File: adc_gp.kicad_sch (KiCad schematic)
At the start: 69 parts

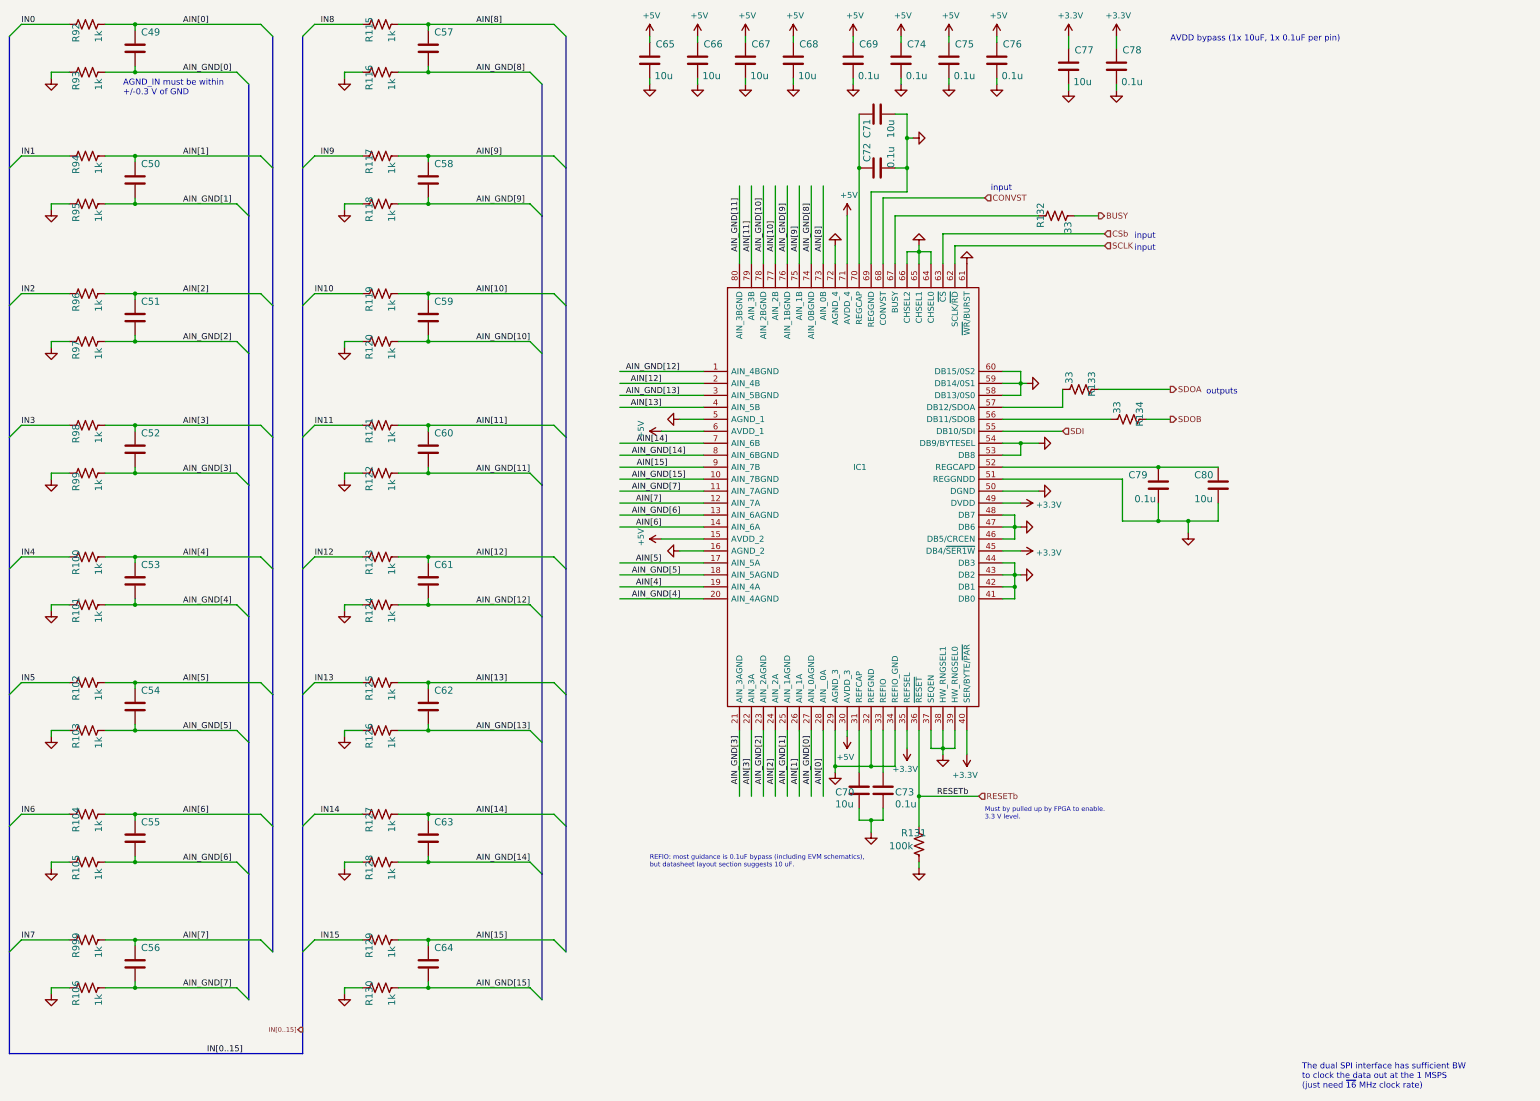
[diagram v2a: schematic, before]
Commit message: Closes #29 full-scale range will be nearly 8uA
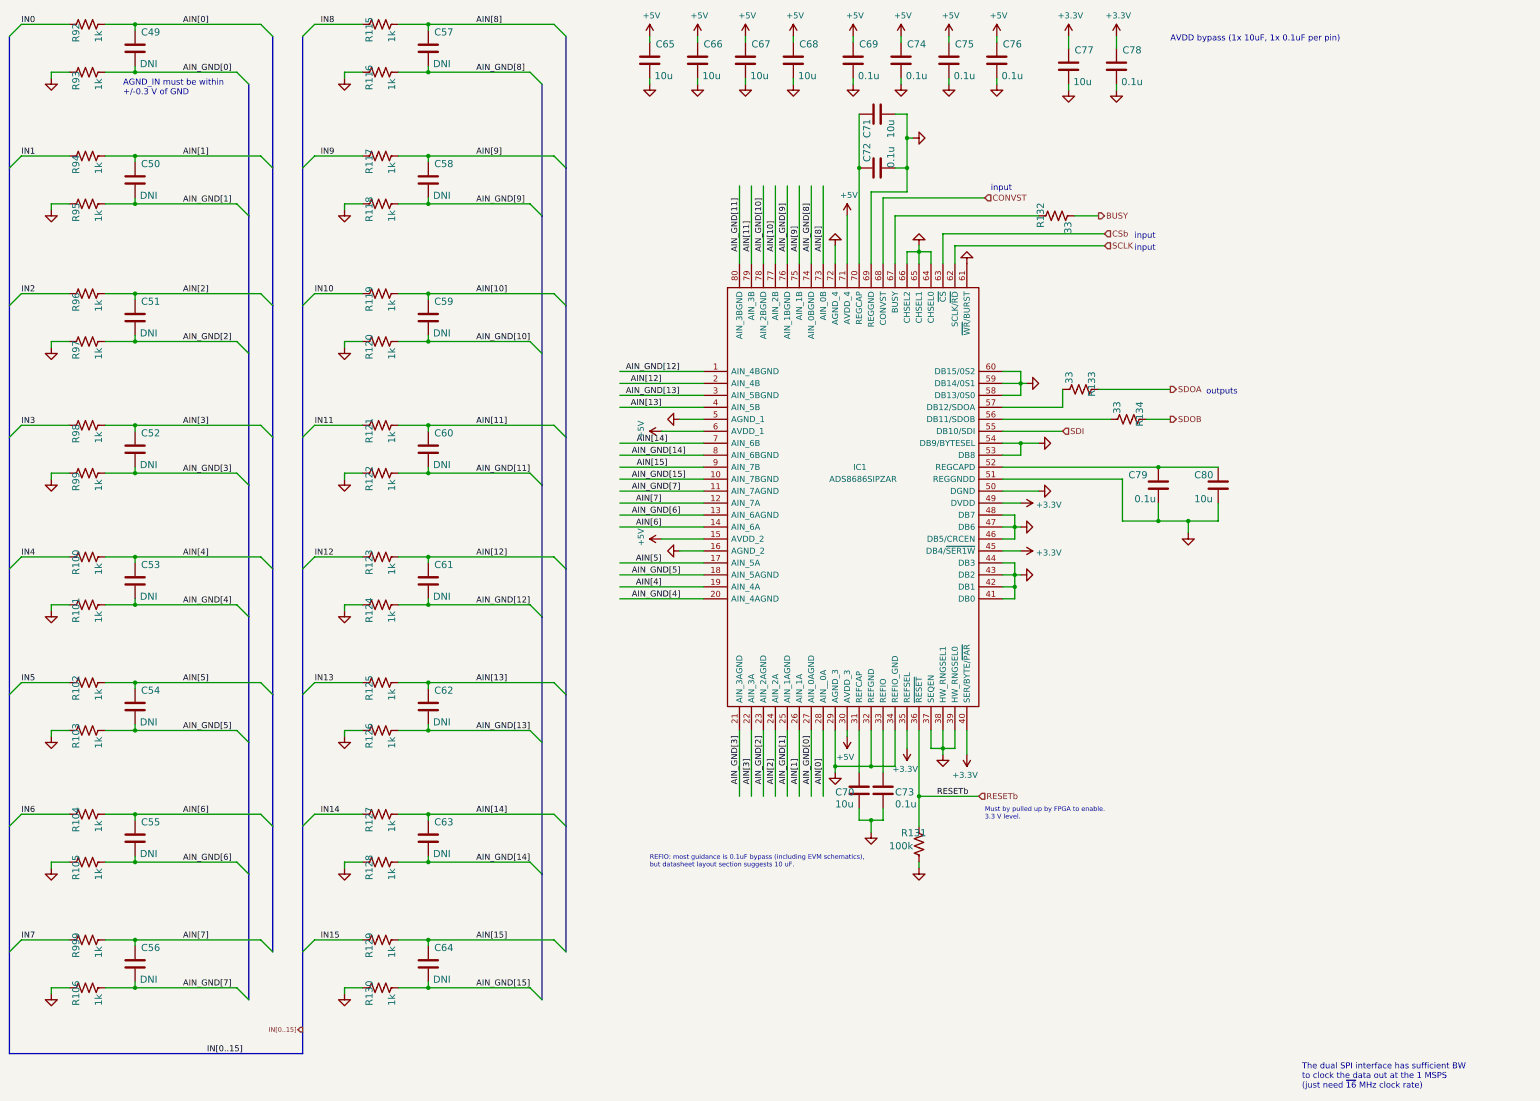
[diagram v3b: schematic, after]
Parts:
- C49, C50, C51, C52, C53, C54, C55, C56, C57, C58, C59, C60, C61, C62, C63, C64: value (none) -> DNI; footprint (none) -> Capacitor_SMD:C_0603_1608Metric
- IC1: value (none) -> ADS8686SIPZAR; footprint (none) -> Package_QFP:LQFP-80_14x14mm_P0.65mm
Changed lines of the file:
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@@
       (effects (font (size 1.27 1.27)) (justify left))
     )
-    (property "Value" "" (id 1) (at 189.23 111.76 0)
+    (property "Value" "ADS8686SIPZAR" (id 1) (at 189.23 111.76 0)
       (effects (font (size 1.27 1.27)) (justify left))
     )
-    (property "Footprint" "" (id 2) (at 222.25 71.12 0)
+    (property "Footprint" "Package_QFP:LQFP-80_14x14mm_P0.65mm" (id 2) (at 222.25 71.12 0)
       (effects (font (size 1.27 1.27)) (justify left) hide)
     )
@@
       (effects (font (size 1.4986 1.4986)) (justify left bottom))
     )
-    (property "Value" "" (id 1) (at 42.926 218.821 0)
-      (effects (font (size 1.4986 1.4986)) (justify left bottom))
-    )
-    (property "Footprint" "" (id 2) (at 41.91 214.63 0)
+    (property "Value" "DNI" (id 1) (at 42.926 218.821 0)
+      (effects (font (size 1.4986 1.4986)) (justify left bottom))
+    )
+    (property "Footprint" "Capacitor_SMD:C_0603_1608Metric" (id 2) (at 41.91 214.63 0)
       (effects (font (size 1.27 1.27)) hide)
     )
@@
       (effects (font (size 1.4986 1.4986)) (justify left bottom))
     )
-    (property "Value" "" (id 1) (at 42.926 192.151 0)
-      (effects (font (size 1.4986 1.4986)) (justify left bottom))
-    )
-    (property "Footprint" "" (id 2) (at 41.91 187.96 0)
+    (property "Value" "DNI" (id 1) (at 42.926 192.151 0)
+      (effects (font (size 1.4986 1.4986)) (justify left bottom))
+    )
+    (property "Footprint" "Capacitor_SMD:C_0603_1608Metric" (id 2) (at 41.91 187.96 0)
       (effects (font (size 1.27 1.27)) hide)
     )
@@
       (effects (font (size 1.4986 1.4986)) (justify left bottom))
     )
-    (property "Value" "" (id 1) (at 42.926 164.211 0)
-      (effects (font (size 1.4986 1.4986)) (justify left bottom))
-    )
-    (property "Footprint" "" (id 2) (at 41.91 160.02 0)
+    (property "Value" "DNI" (id 1) (at 42.926 164.211 0)
+      (effects (font (size 1.4986 1.4986)) (justify left bottom))
+    )
+    (property "Footprint" "Capacitor_SMD:C_0603_1608Metric" (id 2) (at 41.91 160.02 0)
       (effects (font (size 1.27 1.27)) hide)
     )
@@
       (effects (font (size 1.4986 1.4986)) (justify left bottom))
     )
-    (property "Value" "" (id 1) (at 42.926 137.541 0)
-      (effects (font (size 1.4986 1.4986)) (justify left bottom))
-    )
-    (property "Footprint" "" (id 2) (at 41.91 133.35 0)
+    (property "Value" "DNI" (id 1) (at 42.926 137.541 0)
+      (effects (font (size 1.4986 1.4986)) (justify left bottom))
+    )
+    (property "Footprint" "Capacitor_SMD:C_0603_1608Metric" (id 2) (at 41.91 133.35 0)
       (effects (font (size 1.27 1.27)) hide)
     )
@@
       (effects (font (size 1.4986 1.4986)) (justify left bottom))
     )
-    (property "Value" "" (id 1) (at 42.926 109.601 0)
-      (effects (font (size 1.4986 1.4986)) (justify left bottom))
-    )
-    (property "Footprint" "" (id 2) (at 41.91 105.41 0)
+    (property "Value" "DNI" (id 1) (at 42.926 109.601 0)
+      (effects (font (size 1.4986 1.4986)) (justify left bottom))
+    )
+    (property "Footprint" "Capacitor_SMD:C_0603_1608Metric" (id 2) (at 41.91 105.41 0)
       (effects (font (size 1.27 1.27)) hide)
     )
@@
       (effects (font (size 1.4986 1.4986)) (justify left bottom))
     )
-    (property "Value" "" (id 1) (at 42.926 81.661 0)
-      (effects (font (size 1.4986 1.4986)) (justify left bottom))
-    )
-    (property "Footprint" "" (id 2) (at 41.91 77.47 0)
+    (property "Value" "DNI" (id 1) (at 42.926 81.661 0)
+      (effects (font (size 1.4986 1.4986)) (justify left bottom))
+    )
+    (property "Footprint" "Capacitor_SMD:C_0603_1608Metric" (id 2) (at 41.91 77.47 0)
       (effects (font (size 1.27 1.27)) hide)
     )
@@
       (effects (font (size 1.4986 1.4986)) (justify left bottom))
     )
-    (property "Value" "" (id 1) (at 42.926 52.451 0)
-      (effects (font (size 1.4986 1.4986)) (justify left bottom))
-    )
-    (property "Footprint" "" (id 2) (at 41.91 48.26 0)
+    (property "Value" "DNI" (id 1) (at 42.926 52.451 0)
+      (effects (font (size 1.4986 1.4986)) (justify left bottom))
+    )
+    (property "Footprint" "Capacitor_SMD:C_0603_1608Metric" (id 2) (at 41.91 48.26 0)
       (effects (font (size 1.27 1.27)) hide)
     )
@@
       (effects (font (size 1.4986 1.4986)) (justify left bottom))
     )
-    (property "Value" "" (id 1) (at 42.926 24.511 0)
-      (effects (font (size 1.4986 1.4986)) (justify left bottom))
-    )
-    (property "Footprint" "" (id 2) (at 41.91 20.32 0)
+    (property "Value" "DNI" (id 1) (at 42.926 24.511 0)
+      (effects (font (size 1.4986 1.4986)) (justify left bottom))
+    )
+    (property "Footprint" "Capacitor_SMD:C_0603_1608Metric" (id 2) (at 41.91 20.32 0)
       (effects (font (size 1.27 1.27)) hide)
     )
@@
       (effects (font (size 1.4986 1.4986)) (justify left bottom))
     )
-    (property "Value" "" (id 1) (at 105.156 218.821 0)
-      (effects (font (size 1.4986 1.4986)) (justify left bottom))
-    )
-    (property "Footprint" "" (id 2) (at 104.14 214.63 0)
+    (property "Value" "DNI" (id 1) (at 105.156 218.821 0)
+      (effects (font (size 1.4986 1.4986)) (justify left bottom))
+    )
+    (property "Footprint" "Capacitor_SMD:C_0603_1608Metric" (id 2) (at 104.14 214.63 0)
       (effects (font (size 1.27 1.27)) hide)
     )
@@
       (effects (font (size 1.4986 1.4986)) (justify left bottom))
     )
-    (property "Value" "" (id 1) (at 105.156 192.151 0)
-      (effects (font (size 1.4986 1.4986)) (justify left bottom))
-    )
-    (property "Footprint" "" (id 2) (at 104.14 187.96 0)
+    (property "Value" "DNI" (id 1) (at 105.156 192.151 0)
+      (effects (font (size 1.4986 1.4986)) (justify left bottom))
+    )
+    (property "Footprint" "Capacitor_SMD:C_0603_1608Metric" (id 2) (at 104.14 187.96 0)
       (effects (font (size 1.27 1.27)) hide)
     )
@@
       (effects (font (size 1.4986 1.4986)) (justify left bottom))
     )
-    (property "Value" "" (id 1) (at 105.156 164.211 0)
-      (effects (font (size 1.4986 1.4986)) (justify left bottom))
-    )
-    (property "Footprint" "" (id 2) (at 104.14 160.02 0)
+    (property "Value" "DNI" (id 1) (at 105.156 164.211 0)
+      (effects (font (size 1.4986 1.4986)) (justify left bottom))
+    )
+    (property "Footprint" "Capacitor_SMD:C_0603_1608Metric" (id 2) (at 104.14 160.02 0)
       (effects (font (size 1.27 1.27)) hide)
     )
@@
       (effects (font (size 1.4986 1.4986)) (justify left bottom))
     )
-    (property "Value" "" (id 1) (at 105.156 137.541 0)
-      (effects (font (size 1.4986 1.4986)) (justify left bottom))
-    )
-    (property "Footprint" "" (id 2) (at 104.14 133.35 0)
+    (property "Value" "DNI" (id 1) (at 105.156 137.541 0)
+      (effects (font (size 1.4986 1.4986)) (justify left bottom))
+    )
+    (property "Footprint" "Capacitor_SMD:C_0603_1608Metric" (id 2) (at 104.14 133.35 0)
       (effects (font (size 1.27 1.27)) hide)
     )
@@
       (effects (font (size 1.4986 1.4986)) (justify left bottom))
     )
-    (property "Value" "" (id 1) (at 105.156 109.601 0)
-      (effects (font (size 1.4986 1.4986)) (justify left bottom))
-    )
-    (property "Footprint" "" (id 2) (at 104.14 105.41 0)
+    (property "Value" "DNI" (id 1) (at 105.156 109.601 0)
+      (effects (font (size 1.4986 1.4986)) (justify left bottom))
+    )
+    (property "Footprint" "Capacitor_SMD:C_0603_1608Metric" (id 2) (at 104.14 105.41 0)
       (effects (font (size 1.27 1.27)) hide)
     )
@@
       (effects (font (size 1.4986 1.4986)) (justify left bottom))
     )
-    (property "Value" "" (id 1) (at 105.156 81.661 0)
-      (effects (font (size 1.4986 1.4986)) (justify left bottom))
-    )
-    (property "Footprint" "" (id 2) (at 104.14 77.47 0)
+    (property "Value" "DNI" (id 1) (at 105.156 81.661 0)
+      (effects (font (size 1.4986 1.4986)) (justify left bottom))
+    )
+    (property "Footprint" "Capacitor_SMD:C_0603_1608Metric" (id 2) (at 104.14 77.47 0)
       (effects (font (size 1.27 1.27)) hide)
     )
@@
       (effects (font (size 1.4986 1.4986)) (justify left bottom))
     )
-    (property "Value" "" (id 1) (at 105.156 52.451 0)
-      (effects (font (size 1.4986 1.4986)) (justify left bottom))
-    )
-    (property "Footprint" "" (id 2) (at 104.14 48.26 0)
+    (property "Value" "DNI" (id 1) (at 105.156 52.451 0)
+      (effects (font (size 1.4986 1.4986)) (justify left bottom))
+    )
+    (property "Footprint" "Capacitor_SMD:C_0603_1608Metric" (id 2) (at 104.14 48.26 0)
       (effects (font (size 1.27 1.27)) hide)
     )
@@
       (effects (font (size 1.4986 1.4986)) (justify left bottom))
     )
-    (property "Value" "" (id 1) (at 105.156 24.511 0)
-      (effects (font (size 1.4986 1.4986)) (justify left bottom))
-    )
-    (property "Footprint" "" (id 2) (at 104.14 20.32 0)
-      (effects (font (size 1.27 1.27)) hide)
-    )
+    (property "Value" "DNI" (id 1) (at 105.156 24.511 0)
+      (effects (font (size 1.4986 1.4986)) (justify left bottom))
+    )
+    (property "Footprint" "Capacitor_SMD:C_0603_1608Metric" (id 2) (at 104.14 20.32 0)
+      (effects (font (size 1.27 1.27)) hide)
+    )
